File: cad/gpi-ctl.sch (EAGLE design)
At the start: 97 parts, among them CN2 MICROSDPLAIN, CN3 1X4-BIG, J4 1X4-BIG, SW1 SWITCHGT12-THOLE, SW2 SWITCHKMR211, SW3 SWITCHKMR211, U1 STM32F4/64, U2 ACS711, U3 ULN2003, U8 IC_FT230X-SSOP-16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

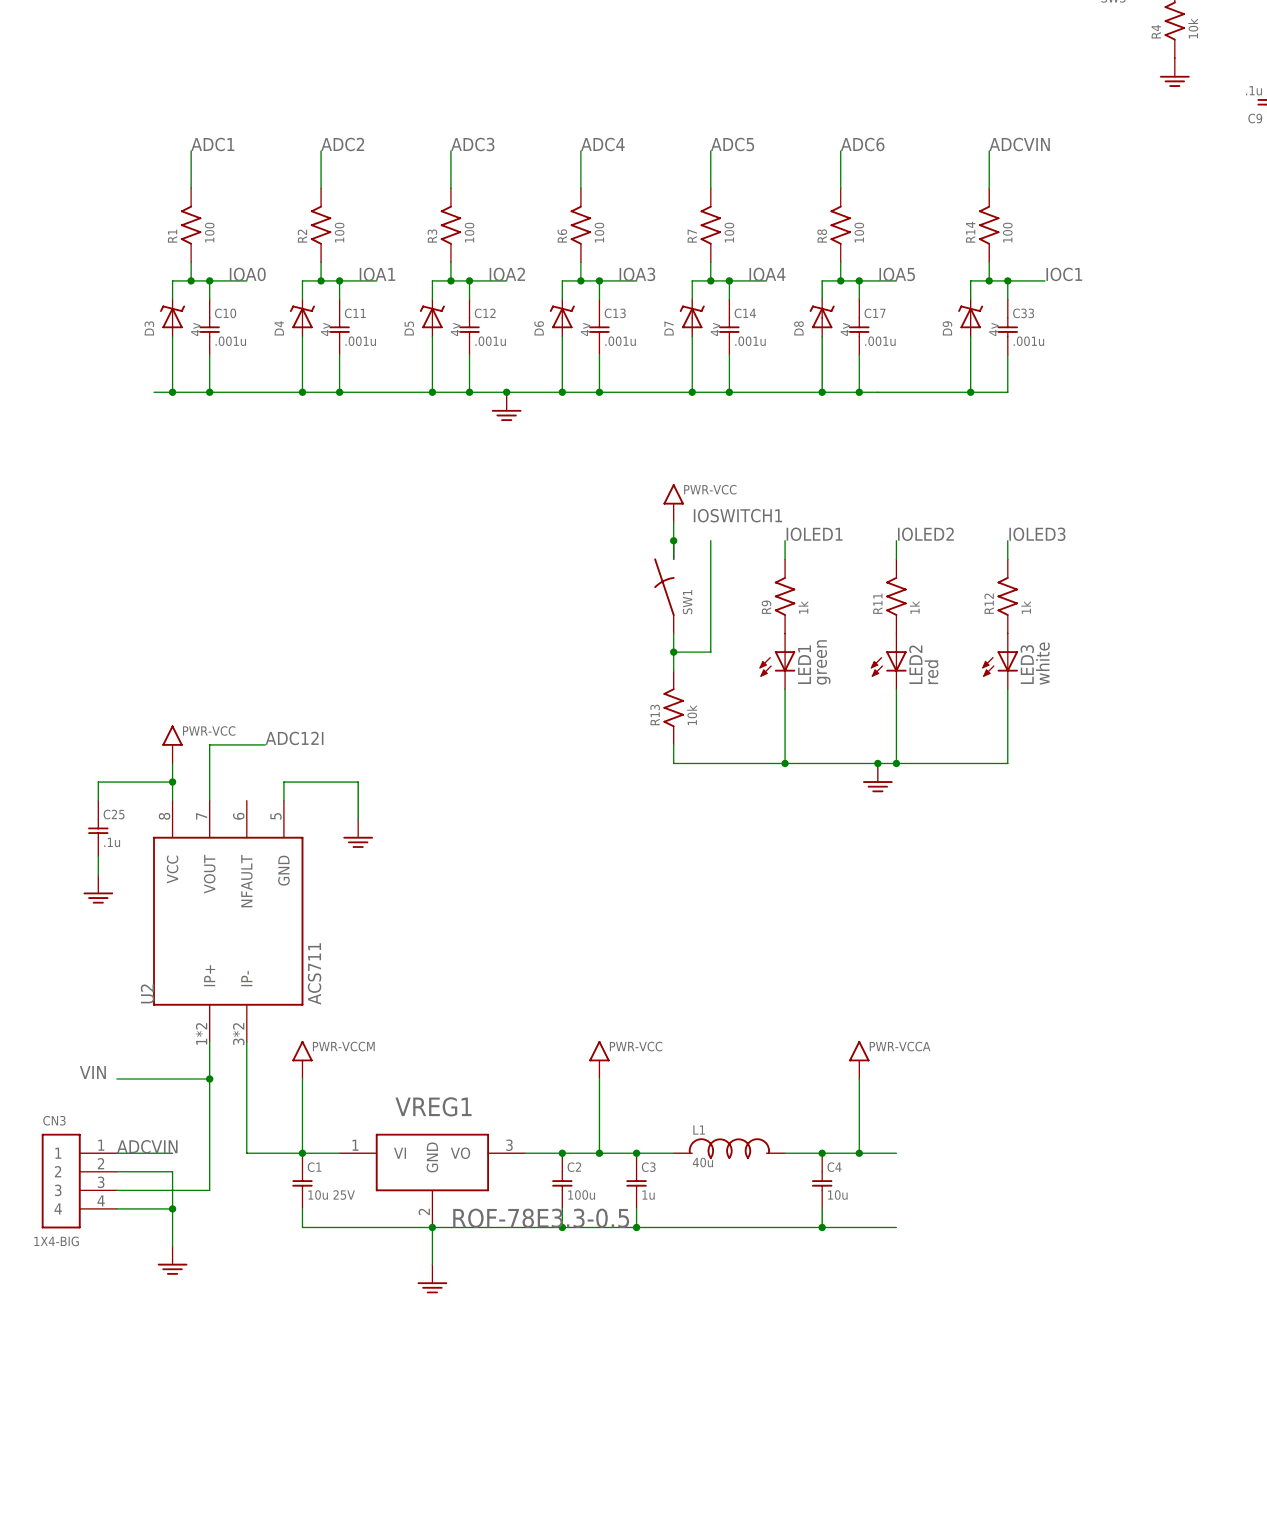
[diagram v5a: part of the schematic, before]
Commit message: op amp on v-div
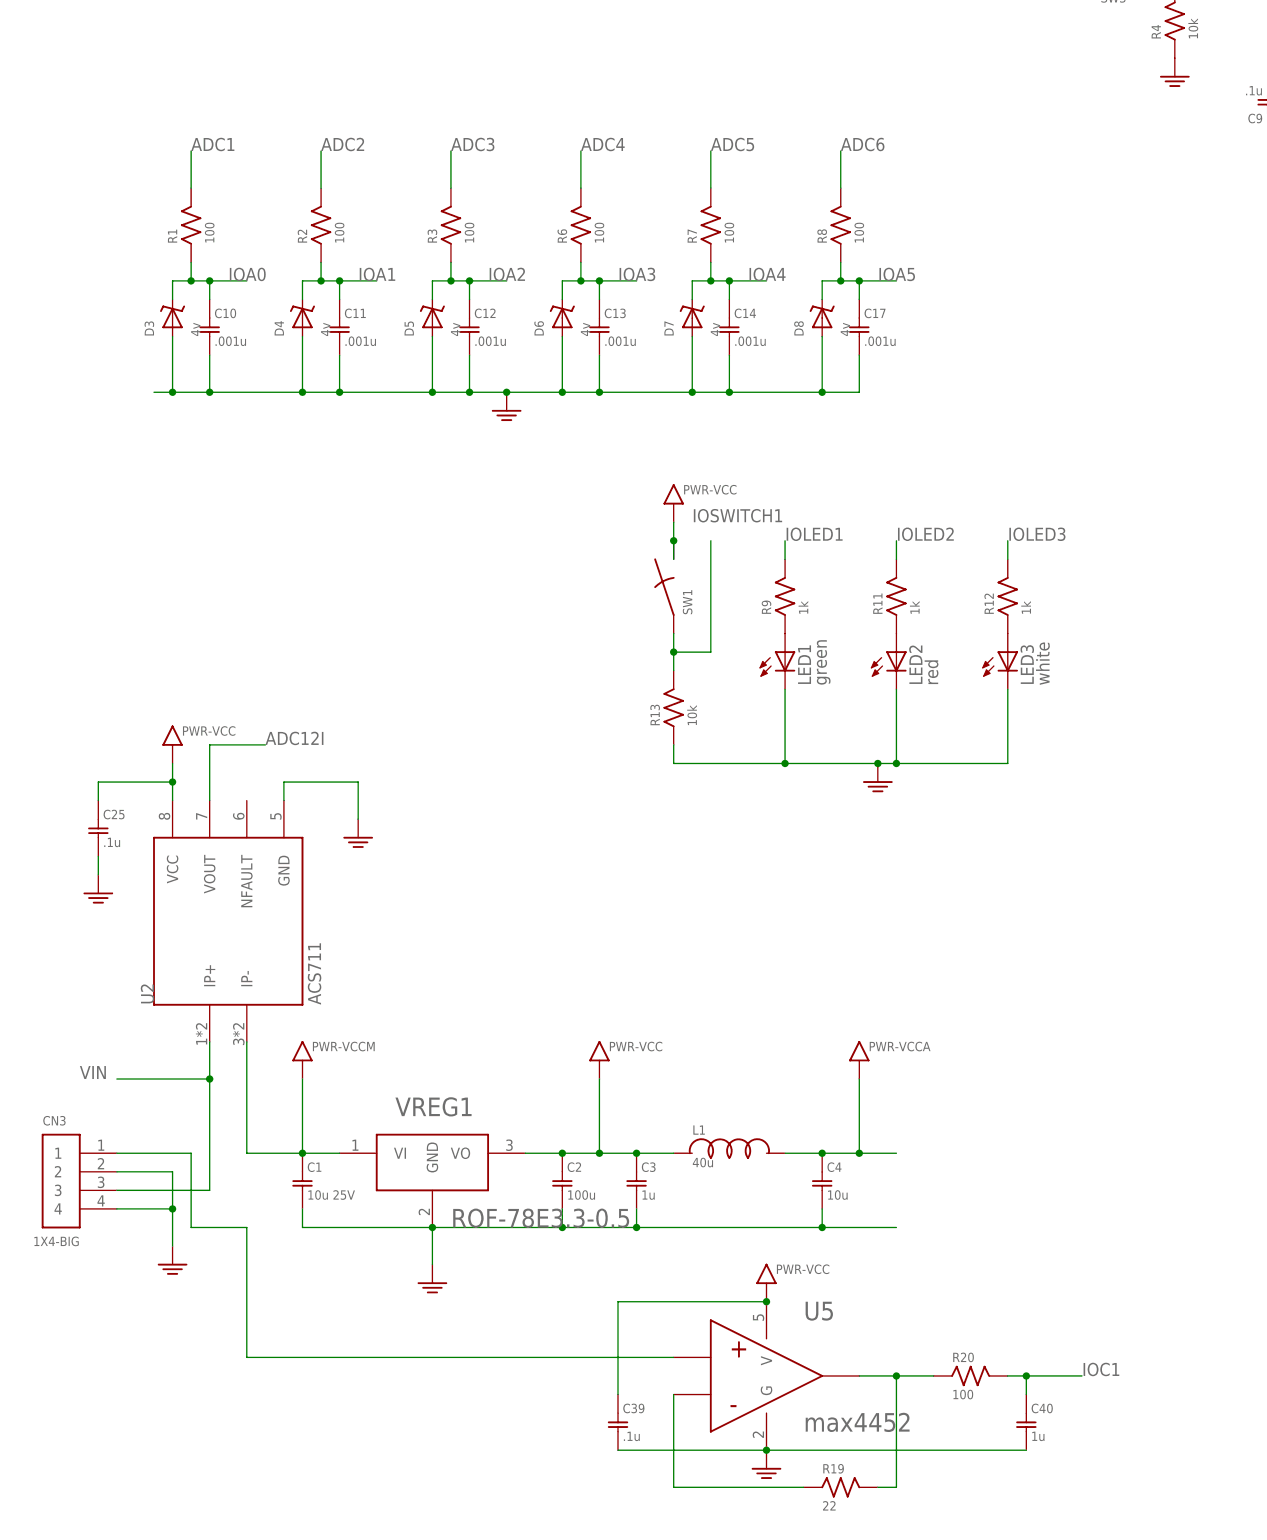
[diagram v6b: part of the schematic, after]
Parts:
- removed C33: .001u, jaw:C0603
- removed D9: 4v, jaw:ZENER
- removed R14: 100, jaw:R0603
- added C39: .1u, jaw:C0603
- added C40: 1u, jaw:C0603
- added R19: 22, jaw:R0603
- added R20: 100, jaw:R0603
- added U5: max4452, jaw:OPAMP
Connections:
- removed net ADCVIN: CN3.1, R14.P$2
- new net N$10: R19.P$1, U5.INM
- new net N$11: R19.P$2, R20.P$1, U5.OUT
- new net N$13: CN3.1, U5.INP
- net GND: now also C39.P$2, C40.P$2, U5.G; no longer C33.P$2, D9.A
- net IOC1: now also C40.P$1, R20.P$2; no longer C33.P$1, D9.C, R14.P$1
- net VCC: now also C39.P$1, U5.V
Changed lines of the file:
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@@
 <part name="C7" library="jaw" deviceset="C" device="0603" value=".1u"/>
 <part name="C32" library="jaw" deviceset="C" device="0603" value=".1u"/>
-<part name="D9" library="jaw" deviceset="ZENER" device="" value="4v"/>
-<part name="C33" library="jaw" deviceset="C" device="0603" value=".001u"/>
-<part name="R14" library="jaw" deviceset="R" device="0603" value="100"/>
 <part name="C34" library="jaw" deviceset="C" device="0603" value=".1u"/>
 <part name="C35" library="jaw" deviceset="C" device="0603" value=".1u"/>
@@
 <part name="R15" library="jaw" deviceset="R" device="0603"/>
 <part name="C38" library="jaw" deviceset="C" device="0603"/>
+<part name="U5" library="jaw" deviceset="OPAMP" device="" value="max4452"/>
+<part name="R19" library="jaw" deviceset="R" device="0603" value="22"/>
+<part name="C39" library="jaw" deviceset="C" device="0603" value=".1u"/>
+<part name="GND27" library="jaw" deviceset="PWR-GND" device=""/>
+<part name="VCC16" library="jaw" deviceset="PWR-VCC" device=""/>
+<part name="R20" library="jaw" deviceset="R" device="0603" value="100"/>
+<part name="C40" library="jaw" deviceset="C" device="0603" value="1u"/>
 </parts>
 <sheets>
@@
 <instance part="C7" gate="G$1" x="58.42" y="251.46"/>
 <instance part="C32" gate="G$1" x="63.5" y="251.46"/>
-<instance part="D9" gate="G$1" x="139.7" y="170.18" rot="R90"/>
-<instance part="C33" gate="G$1" x="144.78" y="167.64"/>
-<instance part="R14" gate="G$1" x="142.24" y="182.88" rot="R90"/>
 <instance part="C34" gate="G$1" x="33.02" y="251.46"/>
 <instance part="C35" gate="G$1" x="27.94" y="251.46"/>
@@
 <instance part="R15" gate="G$1" x="93.98" y="251.46"/>
 <instance part="C38" gate="G$1" x="101.6" y="246.38"/>
+<instance part="U5" gate="G$1" x="111.76" y="25.4"/>
+<instance part="R19" gate="G$1" x="121.92" y="10.16"/>
+<instance part="C39" gate="G$1" x="91.44" y="17.78"/>
+<instance part="GND27" gate="G$1" x="111.76" y="12.7"/>
+<instance part="VCC16" gate="G$1" x="111.76" y="38.1"/>
+<instance part="R20" gate="G$1" x="139.7" y="25.4"/>
+<instance part="C40" gate="G$1" x="147.32" y="17.78"/>
 </instances>
 <busses>
@@
 <wire x1="106.68" y1="160.02" x2="119.38" y2="160.02" width="0.1524" layer="91"/>
 <wire x1="119.38" y1="160.02" x2="124.46" y2="160.02" width="0.1524" layer="91"/>
-<wire x1="124.46" y1="160.02" x2="127" y2="160.02" width="0.1524" layer="91"/>
 <wire x1="30.48" y1="167.64" x2="30.48" y2="160.02" width="0.1524" layer="91"/>
 <junction x="30.48" y="160.02"/>
@@
 <pinref part="C17" gate="G$1" pin="P$2"/>
 <wire x1="124.46" y1="165.1" x2="124.46" y2="160.02" width="0.1524" layer="91"/>
-<junction x="124.46" y="160.02"/>
 <pinref part="GND4" gate="G$1" pin="GND"/>
 <junction x="76.2" y="160.02"/>
-<pinref part="C33" gate="G$1" pin="P$2"/>
-<wire x1="144.78" y1="165.1" x2="144.78" y2="160.02" width="0.1524" layer="91"/>
-<wire x1="144.78" y1="160.02" x2="139.7" y2="160.02" width="0.1524" layer="91"/>
-<pinref part="D9" gate="G$1" pin="A"/>
-<wire x1="139.7" y1="160.02" x2="127" y2="160.02" width="0.1524" layer="91"/>
-<wire x1="139.7" y1="167.64" x2="139.7" y2="160.02" width="0.1524" layer="91"/>
-<junction x="139.7" y="160.02"/>
 </segment>
 <segment>
@@
 <wire x1="332.74" y1="182.88" x2="350.52" y2="182.88" width="0.1524" layer="91"/>
 </segment>
+<segment>
+<pinref part="C39" gate="G$1" pin="P$2"/>
+<pinref part="U5" gate="G$1" pin="G"/>
+<pinref part="GND27" gate="G$1" pin="GND"/>
+<pinref part="C40" gate="G$1" pin="P$2"/>
+<wire x1="147.32" y1="15.24" x2="111.76" y2="15.24" width="0.1524" layer="91"/>
+<junction x="111.76" y="15.24"/>
+<wire x1="91.44" y1="15.24" x2="111.76" y2="15.24" width="0.1524" layer="91"/>
+</segment>
 </net>
 <net name="VCC" class="0">
@@
 <wire x1="332.74" y1="185.42" x2="350.52" y2="185.42" width="0.1524" layer="91"/>
 </segment>
+<segment>
+<pinref part="C39" gate="G$1" pin="P$1"/>
+<pinref part="U5" gate="G$1" pin="V"/>
+<pinref part="VCC16" gate="G$1" pin="VCC"/>
+<wire x1="91.44" y1="22.86" x2="91.44" y2="35.56" width="0.1524" layer="91"/>
+<wire x1="91.44" y1="35.56" x2="111.76" y2="35.56" width="0.1524" layer="91"/>
+<junction x="111.76" y="35.56"/>
+</segment>
 </net>
 <net name="VCCA" class="0">
@@
 </segment>
 </net>
-<net name="ADCVIN" class="0">
-<segment>
-<wire x1="22.86" y1="55.88" x2="30.48" y2="55.88" width="0.1524" layer="91"/>
-<label x="22.86" y="55.88" size="1.778" layer="95"/>
-<pinref part="CN3" gate="G$1" pin="1"/>
-</segment>
-<segment>
-<pinref part="R14" gate="G$1" pin="P$2"/>
-<wire x1="142.24" y1="187.96" x2="142.24" y2="193.04" width="0.1524" layer="91"/>
-<label x="142.24" y="193.04" size="1.778" layer="95"/>
-</segment>
-</net>
 <net name="N$6" class="0">
 <segment>
@@
 <net name="IOC1" class="0">
 <segment>
-<pinref part="D9" gate="G$1" pin="C"/>
-<wire x1="139.7" y1="172.72" x2="139.7" y2="175.26" width="0.1524" layer="91"/>
-<pinref part="C33" gate="G$1" pin="P$1"/>
-<wire x1="139.7" y1="175.26" x2="142.24" y2="175.26" width="0.1524" layer="91"/>
-<wire x1="142.24" y1="175.26" x2="144.78" y2="175.26" width="0.1524" layer="91"/>
-<wire x1="144.78" y1="175.26" x2="144.78" y2="172.72" width="0.1524" layer="91"/>
-<pinref part="R14" gate="G$1" pin="P$1"/>
-<wire x1="142.24" y1="175.26" x2="142.24" y2="177.8" width="0.1524" layer="91"/>
-<junction x="142.24" y="175.26"/>
-<wire x1="144.78" y1="175.26" x2="149.86" y2="175.26" width="0.1524" layer="91"/>
-<junction x="144.78" y="175.26"/>
-<label x="149.86" y="175.26" size="1.778" layer="95"/>
-</segment>
-<segment>
 <pinref part="U1" gate="G$1" pin="PC1"/>
 <wire x1="223.52" y1="147.32" x2="220.98" y2="147.32" width="0.1524" layer="91"/>
 <label x="210.82" y="147.32" size="1.778" layer="95"/>
+</segment>
+<segment>
+<pinref part="R20" gate="G$1" pin="P$2"/>
+<wire x1="144.78" y1="25.4" x2="147.32" y2="25.4" width="0.1524" layer="91"/>
+<pinref part="C40" gate="G$1" pin="P$1"/>
+<wire x1="147.32" y1="25.4" x2="147.32" y2="22.86" width="0.1524" layer="91"/>
+<wire x1="147.32" y1="25.4" x2="154.94" y2="25.4" width="0.1524" layer="91"/>
+<junction x="147.32" y="25.4"/>
+<label x="154.94" y="25.4" size="1.778" layer="95"/>
 </segment>
 </net>
@@
 </segment>
 </net>
+<net name="N$10" class="0">
+<segment>
+<pinref part="U5" gate="G$1" pin="INM"/>
+<pinref part="R19" gate="G$1" pin="P$1"/>
+<wire x1="99.06" y1="22.86" x2="99.06" y2="10.16" width="0.1524" layer="91"/>
+<wire x1="99.06" y1="10.16" x2="116.84" y2="10.16" width="0.1524" layer="91"/>
+</segment>
+</net>
+<net name="N$11" class="0">
+<segment>
+<pinref part="R19" gate="G$1" pin="P$2"/>
+<wire x1="127" y1="10.16" x2="129.54" y2="10.16" width="0.1524" layer="91"/>
+<pinref part="U5" gate="G$1" pin="OUT"/>
+<wire x1="129.54" y1="10.16" x2="129.54" y2="25.4" width="0.1524" layer="91"/>
+<wire x1="129.54" y1="25.4" x2="124.46" y2="25.4" width="0.1524" layer="91"/>
+<wire x1="129.54" y1="25.4" x2="134.62" y2="25.4" width="0.1524" layer="91"/>
+<junction x="129.54" y="25.4"/>
+<pinref part="R20" gate="G$1" pin="P$1"/>
+</segment>
+</net>
+<net name="N$13" class="0">
+<segment>
+<pinref part="CN3" gate="G$1" pin="1"/>
+<wire x1="22.86" y1="55.88" x2="33.02" y2="55.88" width="0.1524" layer="91"/>
+<wire x1="33.02" y1="55.88" x2="33.02" y2="45.72" width="0.1524" layer="91"/>
+<wire x1="33.02" y1="45.72" x2="40.64" y2="45.72" width="0.1524" layer="91"/>
+<pinref part="U5" gate="G$1" pin="INP"/>
+<wire x1="40.64" y1="45.72" x2="40.64" y2="27.94" width="0.1524" layer="91"/>
+<wire x1="40.64" y1="27.94" x2="99.06" y2="27.94" width="0.1524" layer="91"/>
+</segment>
+</net>
